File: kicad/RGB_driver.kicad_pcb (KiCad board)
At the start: 2 copper layers, 17 parts, among them J2 USB_C_Receptacle_USB2.0_16P, SW2 SW_Push_Open_Dual, SW4 SW_Push_Open_Dual, U3 ATtiny85-20P

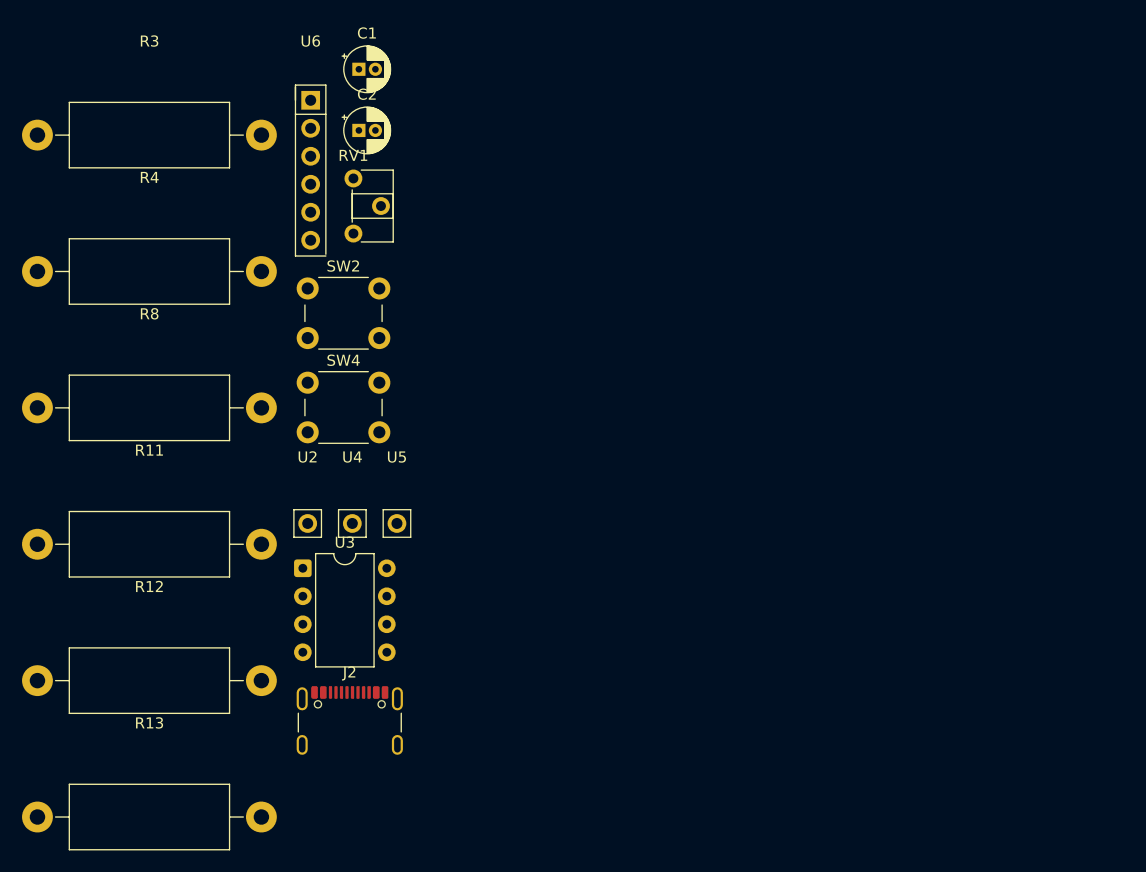
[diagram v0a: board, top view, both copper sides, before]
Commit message: change: added footprints - button, potentiometer, fixed and connected pcb
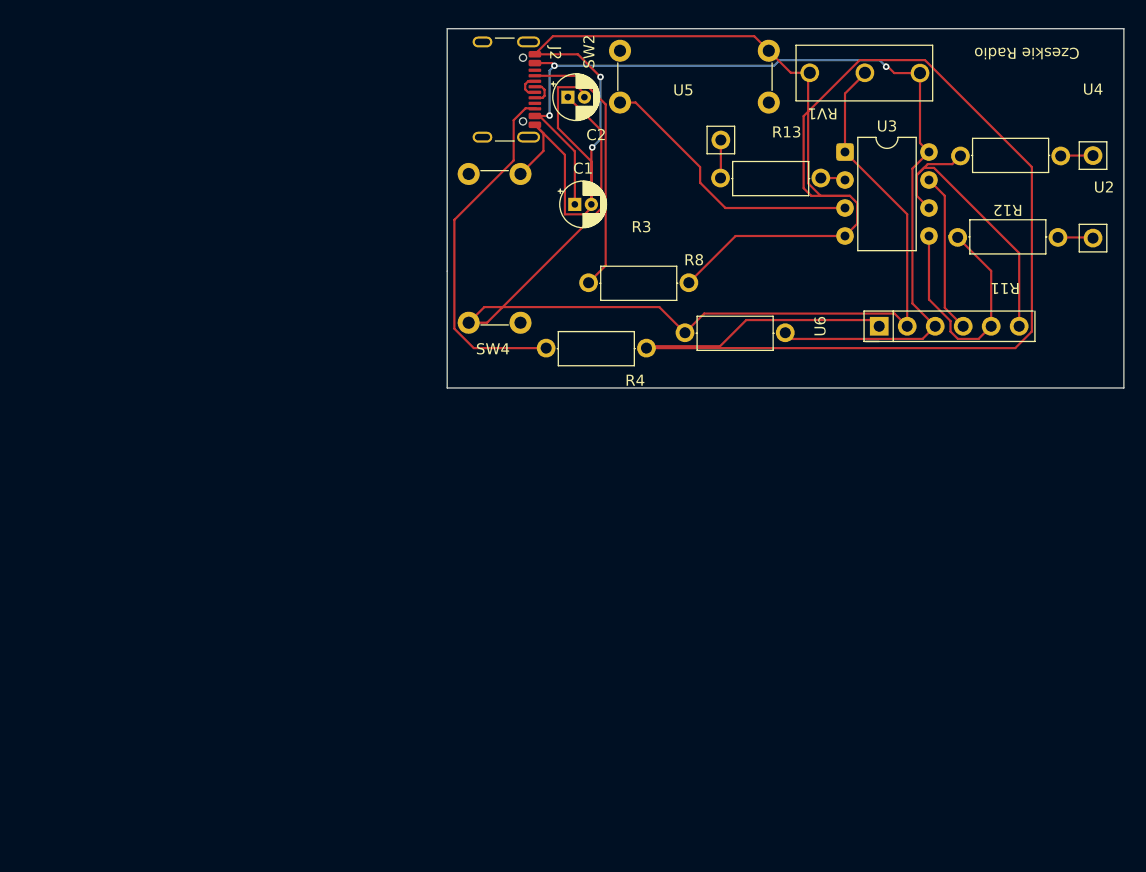
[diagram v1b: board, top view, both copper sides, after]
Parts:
- RV1: footprint Potentiometer_THT:Potentiometer_ACP_CA6-H2,5_Horizontal -> footprint_radiocontorler:potentiometer_custom
- SW2, SW4: footprint Button_Switch_THT:SW_PUSH_6mm -> footprint_radiocontorler:a_long_button
- moved R12 85.5 mm to (147.5, 63.9), turned to 180 degrees
- moved R11 79.2 mm to (147.2, 71.3), turned to 180 degrees
- moved R13 78.5 mm to (126.2, 57.1)
- moved U2 75.8 mm to (155.2, 61.5)
- moved U4 75.0 mm to (155.2, 54.0)
- moved U3 62.0 mm to (132.7, 59.2)
- moved J2 59.8 mm to (100.9, 53.5), turned to -90 degrees
- moved R8 53.5 mm to (123.0, 71.2)
- moved U6 53.2 mm to (131.0, 75.0), turned to 90 degrees
- moved R3 47.8 mm to (114.2, 66.7)
- moved U5 45.5 mm to (121.4, 52.6)
- moved R4 42.1 mm to (110.4, 72.6)
- moved SW2 40.1 mm to (119.1, 52.3), turned to 90 degrees
- moved RV1 38.6 mm to (125.4, 51.8), turned to 90 degrees
- moved C1 23.1 mm to (108.2, 63.9)
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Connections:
- SW4 pad 1: GND -> unconnected-(SW4-Pad1)
- U2 pad 1: (no net) -> Net-(R11-Pad1)
- U4 pad 1: (no net) -> Net-(R12-Pad1)
- U5 pad 1: (no net) -> Net-(R13-Pad1)
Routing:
- net GND: track 0.00 -> 222.3 mm, vias 0 -> 2
- net RST: track 0.00 -> 96.3 mm
- net +5V: track 0.00 -> 90.6 mm, vias 0 -> 3
- net Net-(J2-CC2): track 0.00 -> 32.6 mm
- net Net-(U3-PB1): track 0.00 -> 27.5 mm
- net Net-(U3-XTAL2/PB4): track 0.00 -> 25.2 mm
- net Net-(J2-CC1): track 0.00 -> 24.3 mm
- net Net-(U3-AREF/PB0): track 0.00 -> 24.0 mm
- net Net-(U3-PB2): track 0.00 -> 14.6 mm
- net Net-(R13-Pad1): track 0.00 -> 3.42 mm
- net Net-(R11-Pad1): track 0.00 -> 3.12 mm
- net Net-(J2-D+-PadA6): track 0.00 -> 2.50 mm
- net Net-(J2-D--PadA7): track 0.00 -> 2.44 mm
- net Net-(R12-Pad1): track 0.00 -> 2.40 mm
- net Net-(U3-XTAL1/PB3): track 0.00 -> 2.01 mm
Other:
- board outline added: 61.4 x 32.6 mm
- board text added: "Czeskie Radio"

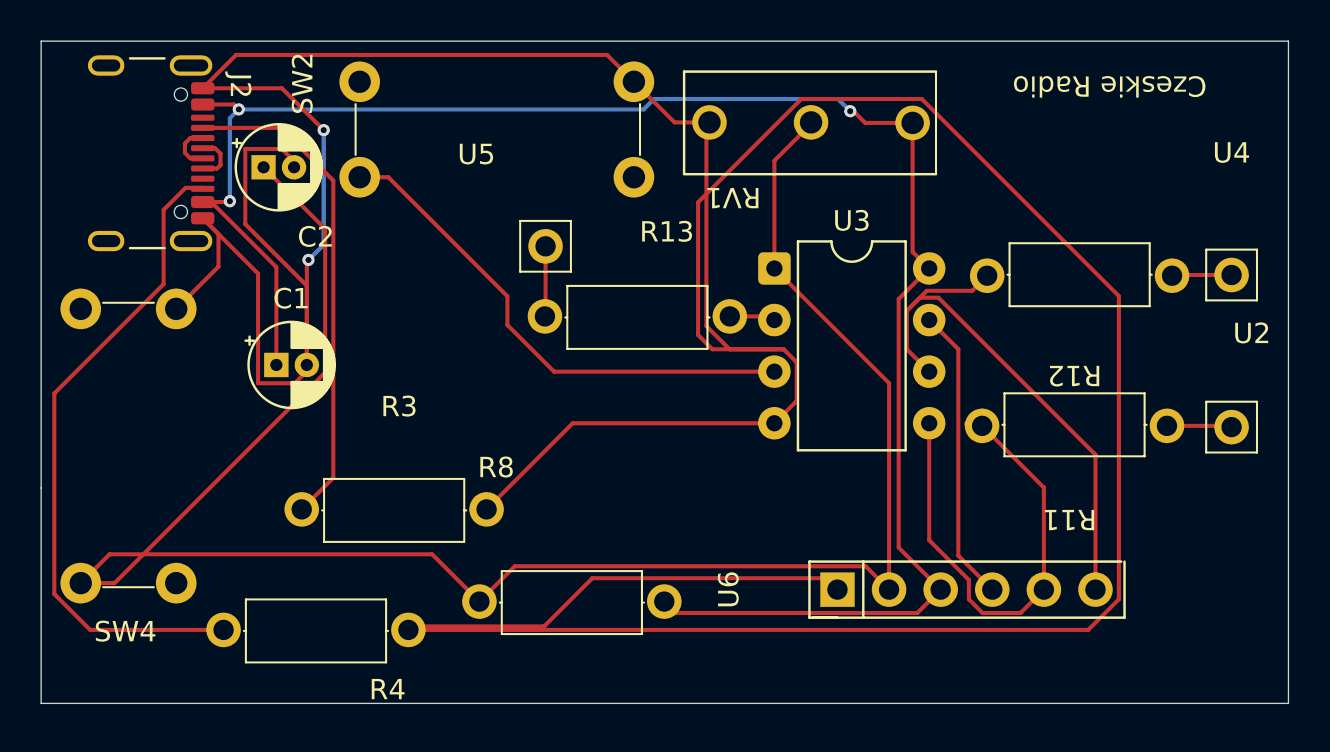
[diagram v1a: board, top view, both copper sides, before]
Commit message: change: corrected button size, reorganized pcb
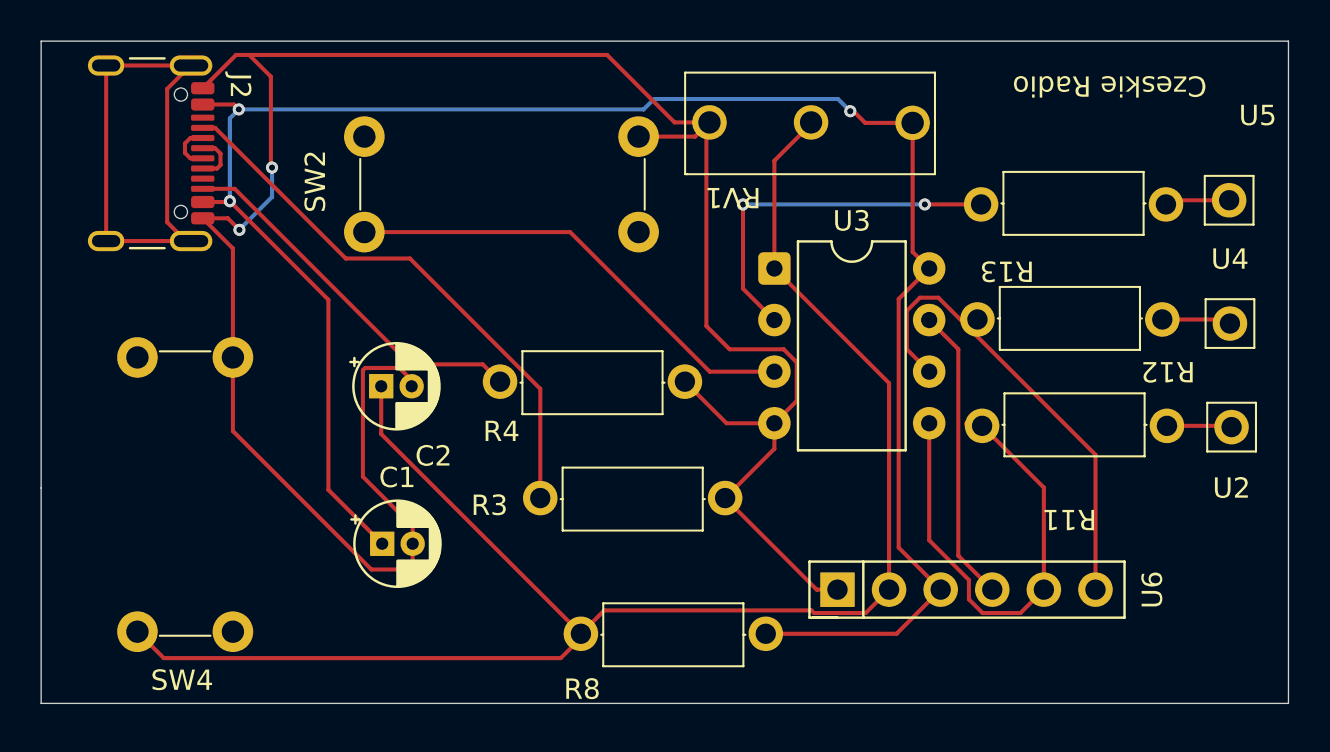
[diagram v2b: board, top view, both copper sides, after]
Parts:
- SW2, SW4: footprint footprint_radiocontorler:a_long_button -> footprint_radiocontorler:a_huge_button
- moved U5 33.7 mm to (155.1, 50.3)
- moved R13 21.2 mm to (147.2, 60.4), turned to 180 degrees
- moved R4 18.3 mm to (124.0, 60.4)
- moved C2 12.2 mm to (113.3, 65.0)
- moved R3 11.8 mm to (126.0, 66.1)
- moved C1 10.2 mm to (113.4, 72.7)
- moved R8 5.24 mm to (128.0, 72.8)
- moved SW4 3.67 mm to (103.6, 70.3)
- moved SW2 2.71 mm to (119.3, 55.0)
- moved U4 2.39 mm to (155.1, 56.4)
- moved R12 2.21 mm to (147.0, 66.1)
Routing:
- net GND: track 222.3 -> 115.2 mm
- net unconnected-(J2-SHIELD-PadS1): track 0.00 -> 26.8 mm
- net Net-(U3-XTAL1/PB3): track 2.01 -> 18.5 mm, vias 0 -> 2
- net RST: track 96.3 -> 81.3 mm
- net Net-(J2-CC2): track 32.6 -> 18.6 mm
- net +5V: track 90.6 -> 96.4 mm
- net Net-(U3-PB1): track 27.5 -> 22.8 mm
- net Net-(J2-CC1): track 24.3 -> 27.3 mm
- net Net-(U3-XTAL2/PB4): track 25.2 -> 23.0 mm
- net Net-(R12-Pad1): track 2.40 -> 3.41 mm

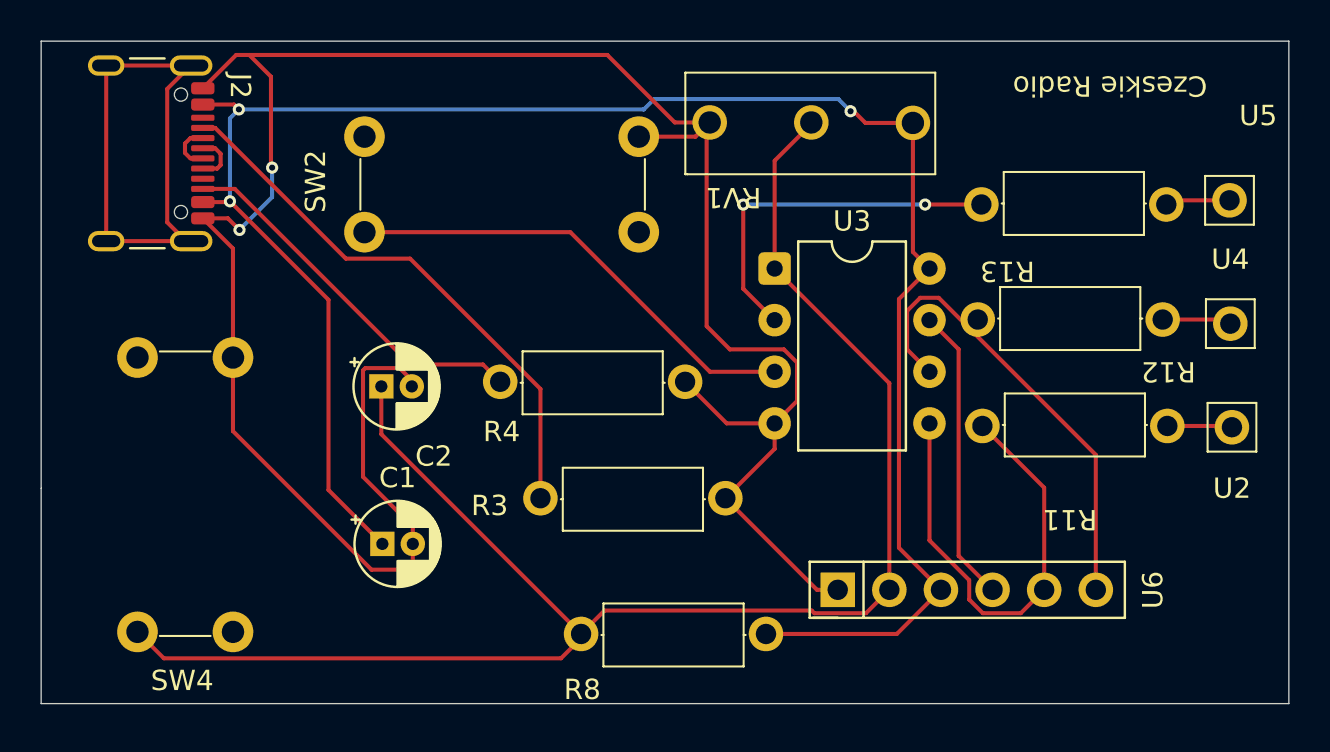
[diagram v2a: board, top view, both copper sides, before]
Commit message: fix: reset, spi, main button and potentiometer changed pins and connections, no capacitor on reset, ceramic capacitor at vcc
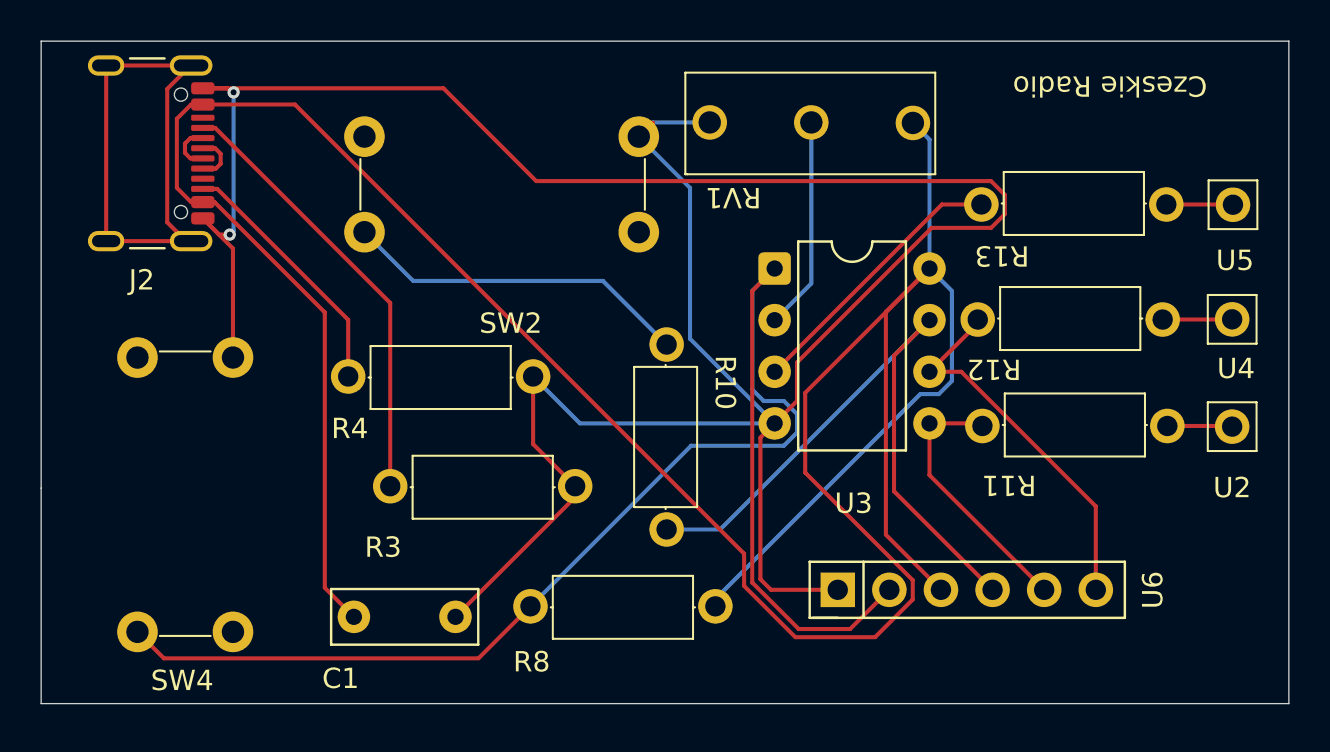
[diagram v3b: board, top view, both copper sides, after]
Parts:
- removed C2: C, Capacitor_THT:CP_Radial_D4.0mm_P1.50mm
- added R10: 1k, footprint_radiocontorler:resistor_footprint, F.Cu at (131.8, 67.7)
- C1: footprint Capacitor_THT:CP_Radial_D4.0mm_P1.50mm -> Capacitor_THT:C_Disc_D7.0mm_W2.5mm_P5.00mm
- moved R4 7.48 mm to (116.5, 60.1)
- moved R3 7.41 mm to (118.6, 65.5)
- moved C1 3.85 mm to (112.0, 76.3)
- moved R8 2.84 mm to (125.5, 71.4)
- moved U5 0.28 mm to (155.2, 50.5)
- moved U4 0.23 mm to (155.2, 56.2)
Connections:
- R13 pad 2: Net-(U3-XTAL1/PB3) -> Net-(U3-XTAL2/PB4)
- RV1 pad 2: RST -> Net-(U3-XTAL1/PB3)
- SW2 pad 1: Net-(U3-XTAL2/PB4) -> Net-(R10-Pad1)
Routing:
- net +5V: track 96.4 -> 146.6 mm, vias 3 -> 0
- net unconnected-(J2-SHIELD-PadS1)_2: track 26.8 -> 0.00 mm
- net unconnected-(J2-SHIELD-PadS1): track 0.00 -> 26.5 mm
- net GND: track 115.2 -> 139.1 mm
- net Net-(U3-PB2): track 14.6 -> 33.2 mm
- net Net-(R10-Pad1): track 0.00 -> 17.2 mm
- net Net-(U3-AREF/PB0): track 24.0 -> 14.0 mm
- net Net-(U3-XTAL2/PB4): track 23.0 -> 13.6 mm
- net RST: track 81.3 -> 72.0 mm
- net Net-(U3-XTAL1/PB3): track 18.5 -> 10.5 mm, vias 2 -> 0
- net Net-(J2-CC2): track 18.6 -> 12.6 mm
- net Net-(J2-CC1): track 27.3 -> 21.8 mm
- net Net-(U3-PB1): track 22.8 -> 18.6 mm

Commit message: fix: power supply for reset removed, new gerber files
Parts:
- removed R8: 10k, footprint_radiocontorler:resistor_footprint
- added U7: ~, footprint_radiocontorler:simple_generic_pad, F.Cu at (155.3, 67.1)
- moved R10 6.95 mm to (125.8, 71.3), turned to 0 degrees
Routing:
- net unconnected-(J2-SHIELD-PadS1): track 26.5 -> 0.00 mm
- net Net-(R10-Pad1): track 17.2 -> 21.8 mm
- net GND: track 139.1 -> 137.0 mm
- net +5V: track 146.6 -> 144.6 mm
- net Net-(U3-PB2): track 33.2 -> 34.2 mm
